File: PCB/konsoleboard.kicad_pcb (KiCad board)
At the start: 2 copper layers, 13 parts, among them SW1 SW_Push, SW10 SW_Push, SW2 SW_Push, SW3 SW_Push, SW4 SW_Push, SW5 SW_Push, SW6 SW_Push, SW7 SW_Push, SW8 SW_Push, SW9 SW_Wuerth_450301014042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

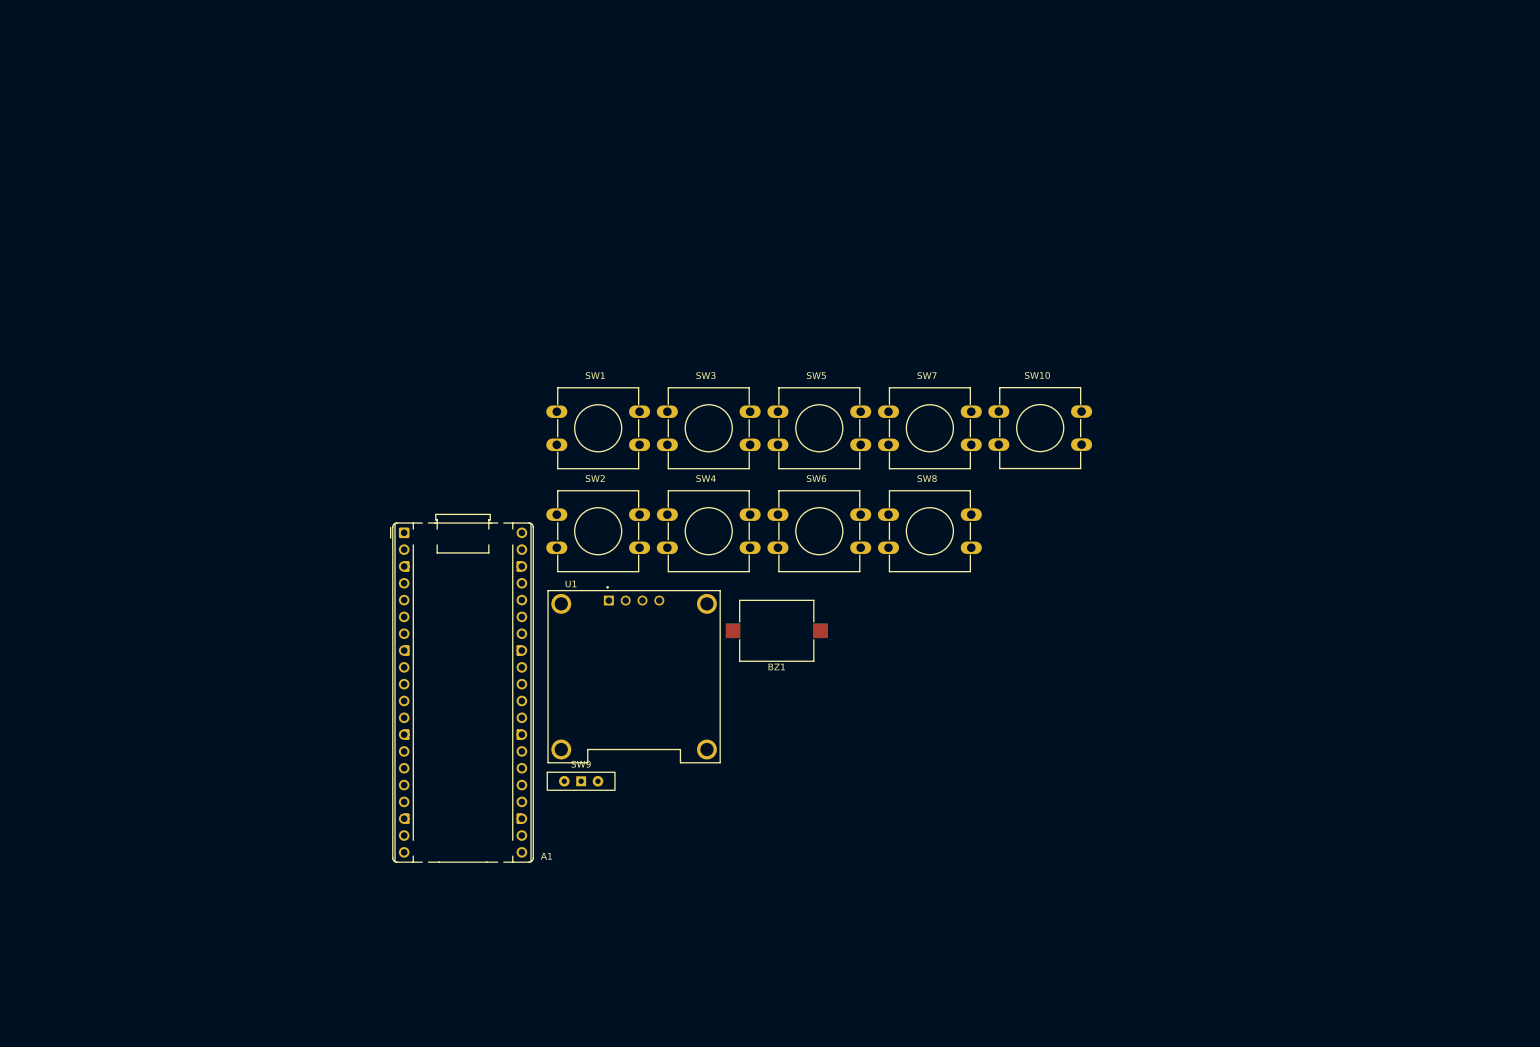
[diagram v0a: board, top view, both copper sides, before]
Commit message: Added 2 more slide switch things for game pause and buzzer toggle, added a bigger display and repositioned most of the components
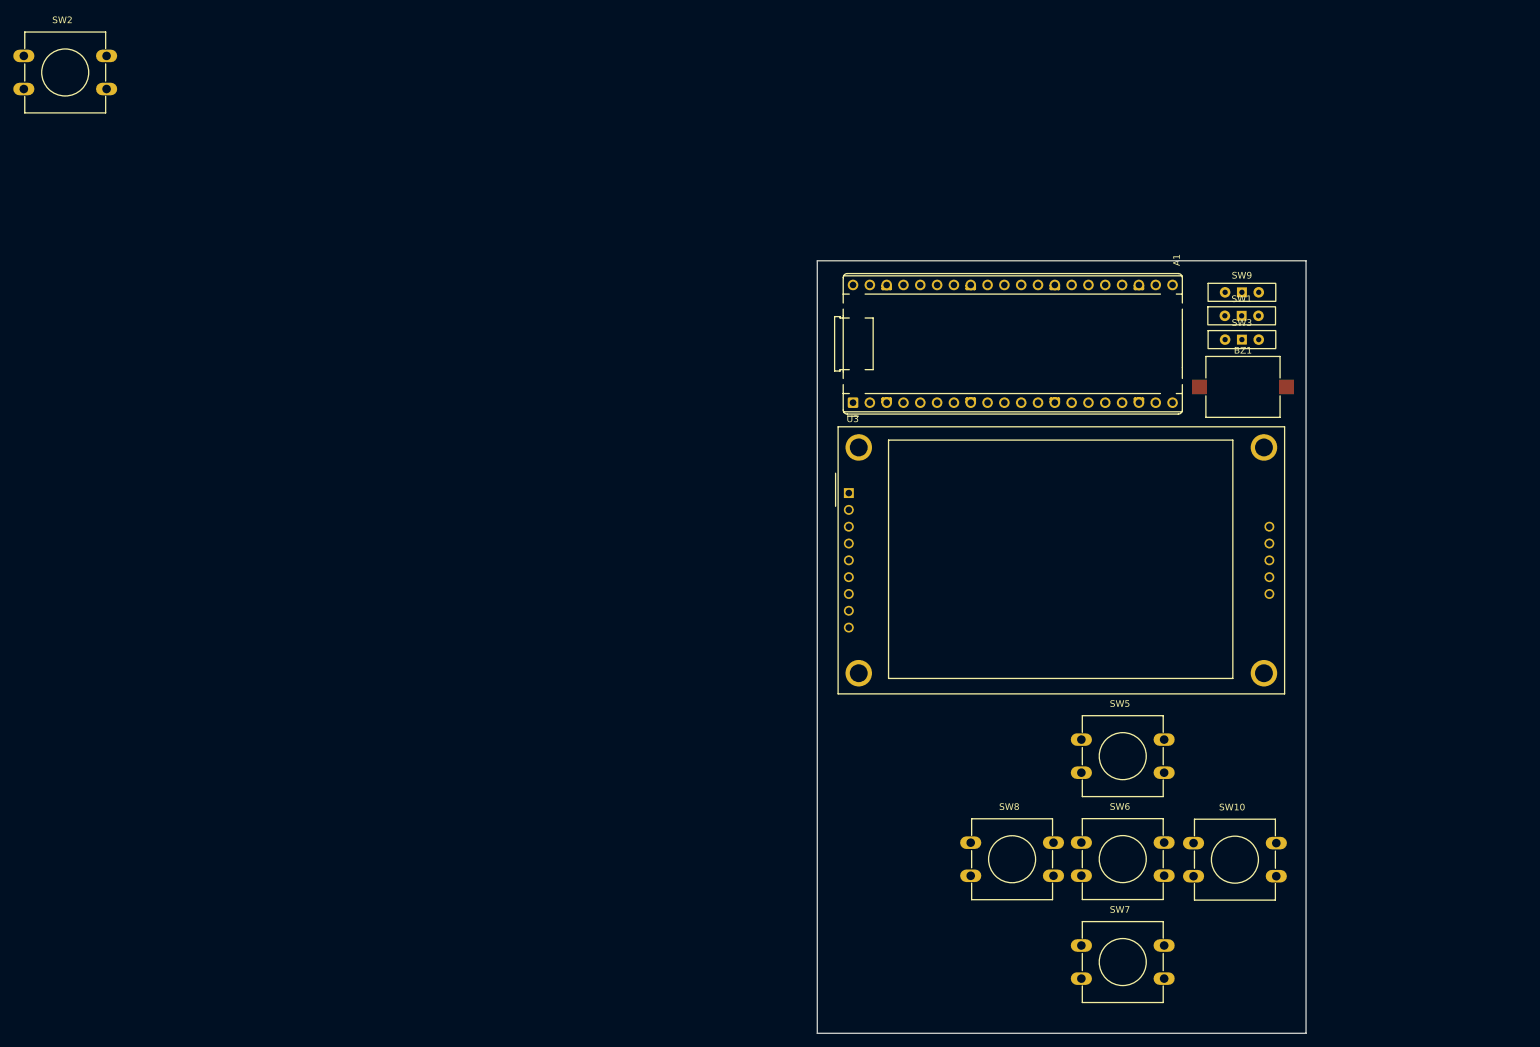
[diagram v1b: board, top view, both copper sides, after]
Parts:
- removed SW4: SW_Push, Button_Switch_THT:SW_PUSH-12mm
- removed U1: DM-OLED096-636, DM-OLED096-636:MODULE_DM-OLED096-636
- added U3: CR2013-MI2120, Display:CR2013-MI2120, F.Cu at (126.2, 70.8)
- SW1, SW3: value SW_Push -> SW_Wuerth_450301014042; footprint Button_Switch_THT:SW_PUSH-12mm -> Button_Switch_THT:SW_Slide-03_Wuerth-WS-SLTV_10x2.5x6.4_P2.54mm
- moved SW9 124.2 mm to (185.6, 40.5)
- moved SW2 106.2 mm to (1.60, 4.78)
- moved SW1 104.4 mm to (185.5, 44.0)
- moved SW3 87.5 mm to (185.6, 47.6)
- moved SW7 85.7 mm to (161.3, 139.1)
- moved BZ1 79.5 mm to (185.7, 54.8), turned to 180 degrees
- moved SW10 71.5 mm to (178.3, 123.7)
- moved A1 70.6 mm to (126.8, 57.1), turned to 90 degrees
- moved SW5 67.5 mm to (161.3, 108.0)
- moved SW6 67.5 mm to (161.3, 123.6)
- moved SW8 51.1 mm to (144.6, 123.6)
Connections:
- A1 pad 1: unconnected-(A1-GPIO0-Pad1) -> SDA2
- A1 pad 2: LP1 -> SCL2
- A1 pad 21: unconnected-(A1-GPIO16-Pad21) -> BuzzerToggleSwitch
- A1 pad 22: unconnected-(A1-GPIO17-Pad22) -> GameToggleSwitch
- A1 pad 4: LP2 -> unconnected-(A1-GPIO2-Pad4)
- A1 pad 5: LP3 -> unconnected-(A1-GPIO3-Pad5)
- A1 pad 6: LP4 -> RP6
- SW1 pad 1: GND -> +3V3
- SW1 pad 2: LP1 -> BuzzerToggleSwitch
- SW2 pad 2: LP2 -> RP6
- SW3 pad 1: GND -> +3V3
- SW3 pad 2: LP3 -> GameToggleSwitch
- SW9 pad 2: ToggleSwitch -> PowerToggleSwitch
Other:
- board outline added: 73.8 x 116.7 mm

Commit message: Completed the pcb routing
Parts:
- moved SW2 202.2 mm to (175.5, 107.9)
- moved A1 3.58 mm to (123.3, 57.1)
- moved SW3 3.37 mm to (183.2, 45.2)
- moved SW9 3.37 mm to (183.2, 38.1)
- moved BZ1 3.37 mm to (183.4, 52.4)
- moved SW1 3.37 mm to (183.2, 41.6)
- moved SW5 2.81 mm to (158.5, 108.0)
- moved SW6 2.81 mm to (158.5, 123.5)
- moved SW7 2.81 mm to (158.5, 139.1)
- moved U3 2.81 mm to (123.4, 70.8)
- moved SW10 2.81 mm to (175.5, 123.6)
- moved SW8 2.81 mm to (141.8, 123.6)
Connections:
- A1 pad 1: SDA2 -> Net-(A1-GPIO0)
- A1 pad 10: RP3 -> RP2
- A1 pad 11: RP4 -> RP1
- A1 pad 12: RP5 -> Net-(A1-GPIO9)
- A1 pad 14: SDA -> GameToggleSwitch
- A1 pad 15: SCL -> BuzzerToggleSwitch
- A1 pad 16: BuzzerP -> Net-(A1-GPIO12)
- A1 pad 17: unconnected-(A1-GPIO13-Pad17) -> Net-(A1-GPIO13)
- A1 pad 2: SCL2 -> BuzzerP
- A1 pad 21: BuzzerToggleSwitch -> MISO
- A1 pad 22: GameToggleSwitch -> unconnected-(A1-GPIO17-Pad22)
- A1 pad 24: unconnected-(A1-GPIO18-Pad24) -> SCK
- A1 pad 25: unconnected-(A1-GPIO19-Pad25) -> MOSI
- A1 pad 27: unconnected-(A1-GPIO21-Pad27) -> FLASH_CD
- A1 pad 29: unconnected-(A1-GPIO22-Pad29) -> SD_CS
- A1 pad 37: ToggleSwitch -> PowerToggleSwitch
- A1 pad 5: unconnected-(A1-GPIO3-Pad5) -> RP6
- A1 pad 6: RP6 -> RP5
- A1 pad 7: RP1 -> RP4
- A1 pad 9: RP2 -> RP3
- U3 pad 1: unconnected-(U3-VCC-Pad1) -> +3V3
- U3 pad 10: unconnected-(U3-SD_CS-Pad10) -> SD_CS
- U3 pad 11: unconnected-(U3-SD_MOSI-Pad11) -> MOSI
- U3 pad 12: unconnected-(U3-SD_MISO-Pad12) -> MISO
- U3 pad 13: unconnected-(U3-SD_SCK-Pad13) -> SCK
- U3 pad 14: unconnected-(U3-FLASH_CD-Pad14) -> FLASH_CD
- U3 pad 3: unconnected-(U3-~{CS}-Pad3) -> Net-(A1-GPIO9)
- U3 pad 4: unconnected-(U3-RESET-Pad4) -> Net-(A1-GPIO12)
- U3 pad 5: unconnected-(U3-D/~{C}-Pad5) -> Net-(A1-GPIO0)
- U3 pad 6: unconnected-(U3-MOSI-Pad6) -> MOSI
- U3 pad 7: unconnected-(U3-SCK-Pad7) -> SCK
- U3 pad 8: unconnected-(U3-LED-Pad8) -> Net-(A1-GPIO13)
- U3 pad 9: unconnected-(U3-MISO-Pad9) -> MISO
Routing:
- net GND: track 0.00 -> 330.9 mm, vias 0 -> 9
- net SCK: track 0.00 -> 123.0 mm, vias 0 -> 3
- net RP3: track 0.00 -> 121.9 mm, vias 0 -> 1
- net RP5: track 0.00 -> 121.6 mm, vias 0 -> 5
- net MISO: track 0.00 -> 117.2 mm, vias 0 -> 1
- net RP1: track 0.00 -> 108.3 mm, vias 0 -> 3
- net MOSI: track 0.00 -> 106.0 mm, vias 0 -> 2
- net RP2: track 0.00 -> 105.1 mm, vias 0 -> 4
- net RP6: track 0.00 -> 104.7 mm, vias 0 -> 4
- net +3V3: track 0.00 -> 94.0 mm
- net RP4: track 0.00 -> 90.5 mm, vias 0 -> 2
- net BuzzerP: track 0.00 -> 88.0 mm, vias 0 -> 5
- net SD_CS: track 0.00 -> 65.0 mm, vias 0 -> 2
- net FLASH_CD: track 0.00 -> 63.8 mm, vias 0 -> 4
- net Net-(A1-GPIO13): track 0.00 -> 53.5 mm
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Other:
- board size 73.8 x 116.7 mm -> 71.9 x 117 mm

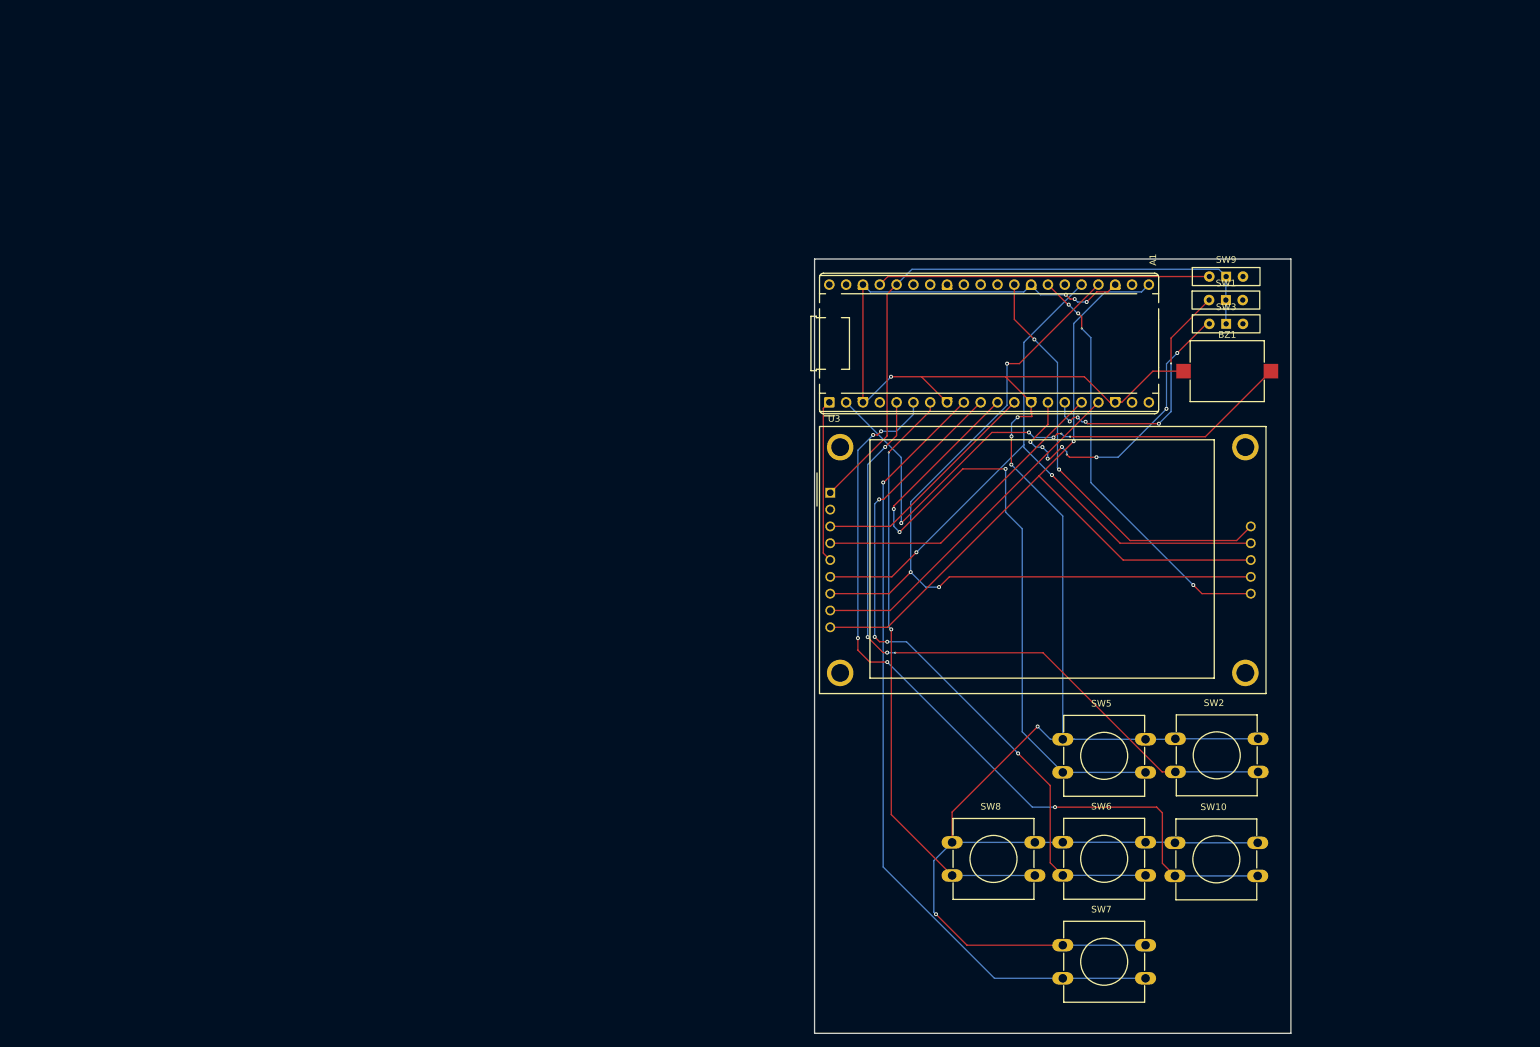
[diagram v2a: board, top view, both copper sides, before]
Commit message: Added Branding and Filled Zone
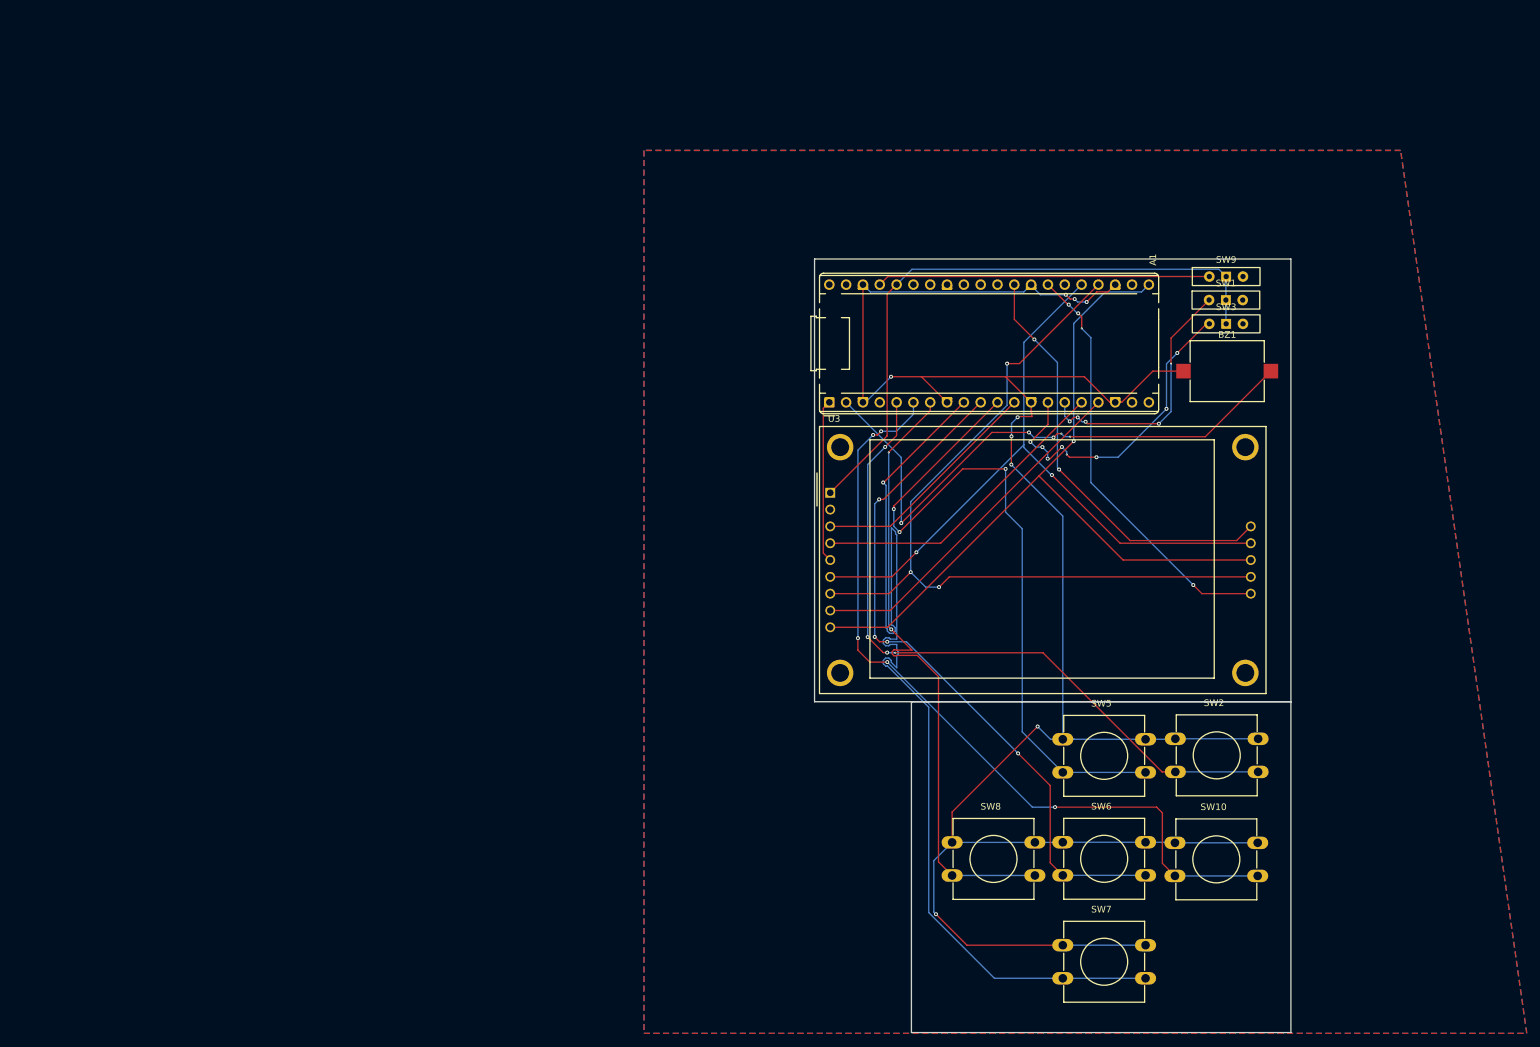
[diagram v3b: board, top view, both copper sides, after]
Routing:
- net RP3: track 121.9 -> 164.2 mm
- net RP4: track 90.5 -> 96.8 mm
- added copper zone on B.Cu, net (none)
- added copper zone on F.Cu, net (none)
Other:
- board size 71.9 x 117 mm -> 71.9 x 116.8 mm
- board text added: "Konsole"
- board text added: "by Faizeen Hoque"
- board text added: "https://faizeenhoque.xyz/"

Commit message: Decided to remove the buzzer and the buzzer switch
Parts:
- removed BZ1: Buzzer, Buzzer_Beeper:Buzzer_Mallory_AST1109MLTRQ
- removed SW1: SW_Wuerth_450301014042, Button_Switch_THT:SW_Slide-03_Wuerth-WS-SLTV_10x2.5x6.4_P2.54mm
- moved SW3 5.29 mm to (183.2, 40.0)
- moved SW9 5.26 mm to (183.1, 43.4)
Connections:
- A1 pad 15: BuzzerToggleSwitch -> unconnected-(A1-GPIO11-Pad15)
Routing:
- net BuzzerP: track 88.0 -> 0.00 mm, vias 5 -> 0
- net BuzzerToggleSwitch: track 39.1 -> 0.00 mm, vias 5 -> 0
- net PowerToggleSwitch: track 50.3 -> 70.2 mm, vias 0 -> 5
- net GND: track 330.9 -> 318.6 mm
- net GameToggleSwitch: track 49.6 -> 56.3 mm
- net +3V3: track 94.0 -> 92.1 mm
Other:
- board text added: "If you are reading this, you are really cool"
